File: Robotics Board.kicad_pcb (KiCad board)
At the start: 2 copper layers, 91 parts, among them CON1 DC_IN, J1 USB, K1 CONN_3, K2 CONN_3, P1 CONN_3, P10 CONN_6, P11 CONN_8, P12 CONN_12, P13 CONN_6, P14 CONN_12, P15 CONN_5, P16 CONN_12, P17 CONN_12, P18 CONN_12, P19 CONN_12, P2 CONN_3, P20 CONN_12, P21 CONN_12, P22 CONN_12, P23 CONN_1, P3 CONN_12, P4 CONN_12, P5 CONN_12, P6 CONN_12, P7 CONN_12, P8 CONN_8, P9 CONN_8, U1 7805, U2 L293, U3 PIC18F4550, U4 FT230X, X1 4MHz

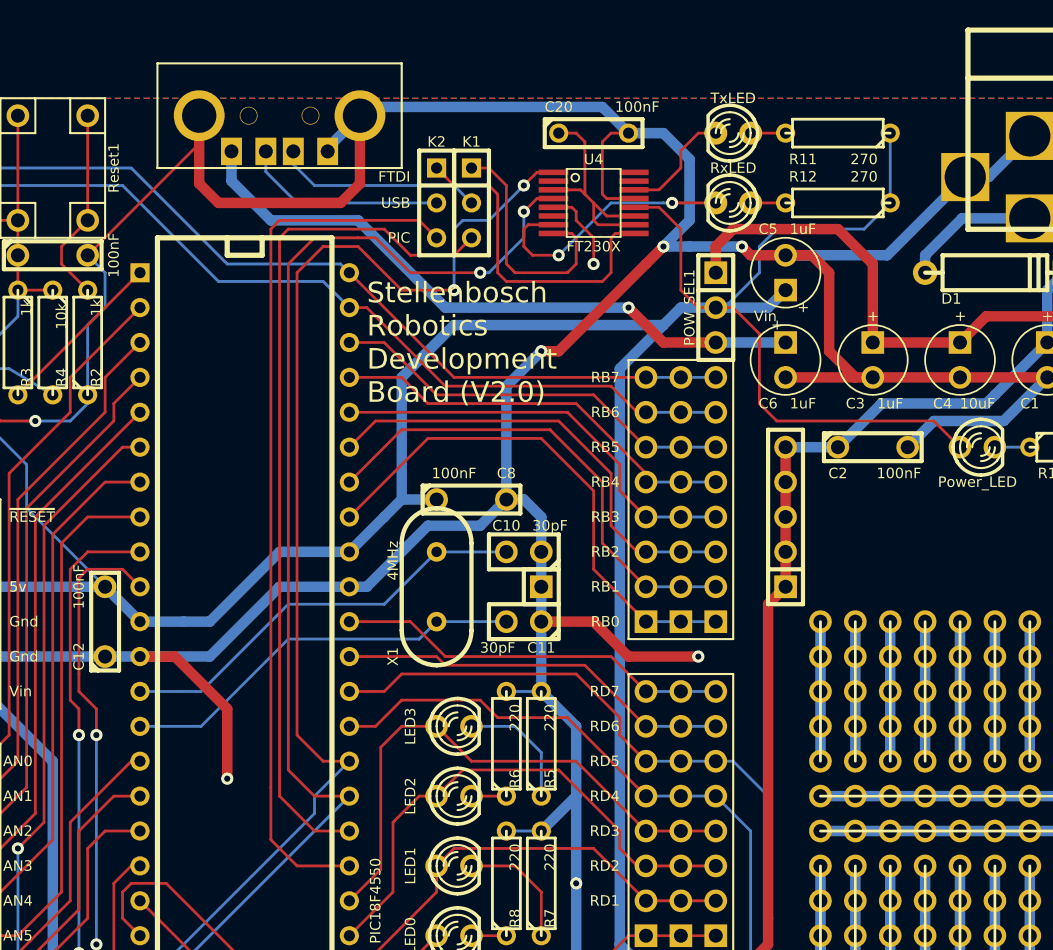
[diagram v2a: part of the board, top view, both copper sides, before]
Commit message: Eddited USB circuit to include resistors and capacitors.
Signed-off-by: Kolijn Wolfaardt <kolijn.wolfaardt@gmail.com>
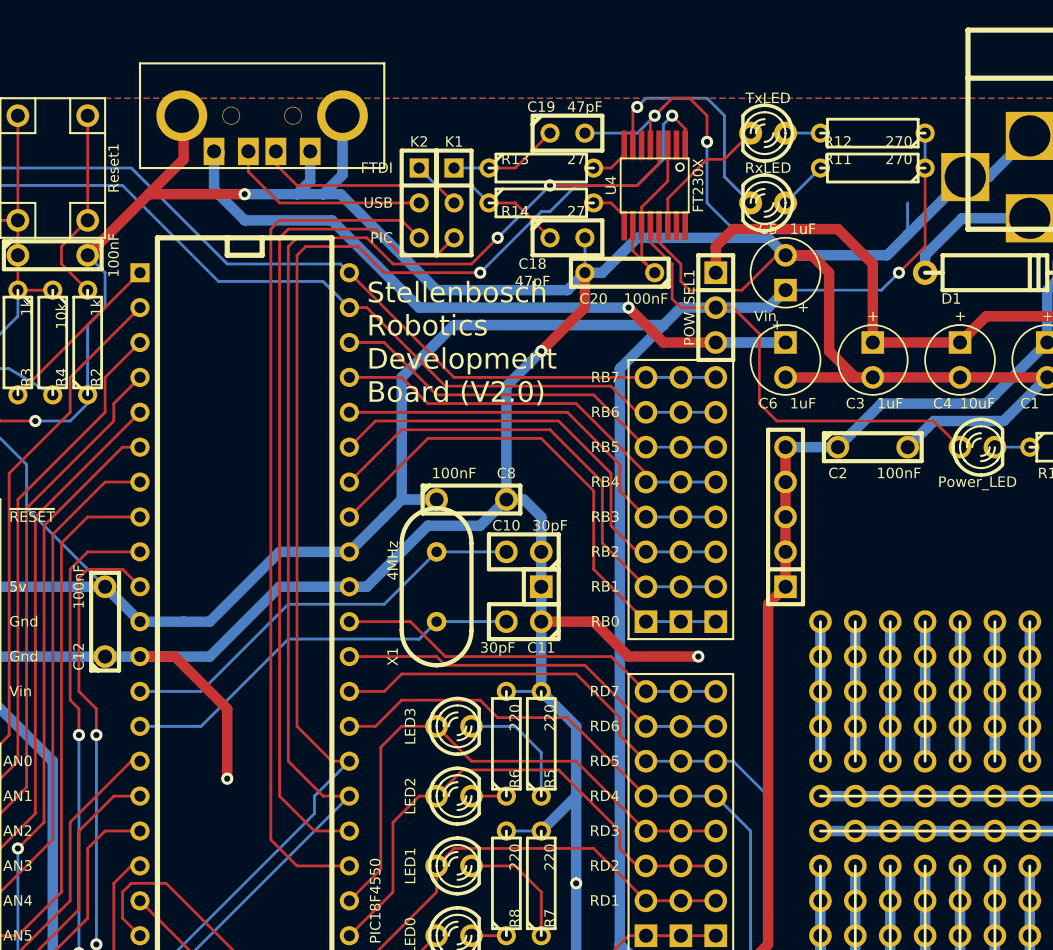
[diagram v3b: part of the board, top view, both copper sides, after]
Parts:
- added C18: 47pF, C1, F.Cu at (111.1, 62.2)
- added C19: 47pF, C1, F.Cu at (111.1, 54.6)
- added R13: 27, R3, F.Cu at (109.2, 57.1)
- added R14: 27, R3, F.Cu at (109.2, 59.7)
- moved C20 10.3 mm to (114.9, 64.8), turned to 180 degrees
- moved U4 4.62 mm to (117.5, 58.4), turned to 180 degrees
- moved R12 3.59 mm to (133.3, 57.1)
- moved D11 2.54 mm to (125.7, 54.6)
- moved D12 2.54 mm to (125.7, 59.7)
- moved R11 2.54 mm to (133.3, 54.6)
- moved J1 1.27 mm to (88.9, 53.3)
- moved K1 1.27 mm to (102.9, 59.7)
- moved K2 1.27 mm to (100.3, 59.7)
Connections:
- U4 pad 8: /Microcontroller/USB_D+ -> N-0000099
- U4 pad 9: /Microcontroller/USB_D- -> N-0000098
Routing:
- net Gnd: track 595.5 -> 611.4 mm
- net /Microcontroller/USB_D-: track 24.1 -> 11.6 mm
- net /Microcontroller/GP7: track 122.4 -> 133.5 mm
- net /Microcontroller/USB_D+: track 18.1 -> 8.04 mm
- net /Microcontroller/GP6: track 119.1 -> 127.9 mm
- net V_5v: track 345.4 -> 340.9 mm, vias 1 -> 2
- net N-0000098: track 0.00 -> 3.32 mm
- net N-0000099: track 0.00 -> 3.32 mm
- net /Microcontroller/VCCIO: track 16.9 -> 13.6 mm
- net /Microcontroller/CBUS2: track 19.4 -> 17.2 mm, vias 2 -> 1
- net /Microcontroller/CBUS1: track 8.42 -> 9.97 mm
- net /Microcontroller/PIC_USB_D+: track 62.3 -> 61.1 mm
- net /Microcontroller/PIC_USB_D-: track 63.8 -> 62.5 mm
- net Vbus: track 47.9 -> 49.2 mm
- net N-0000094: track 2.54 -> 3.59 mm

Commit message: Fixed some small errors
Signed-off-by: Kolijn Wolfaardt <kolijn.wolfaardt@gmail.com>
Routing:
- net V_5v: track 340.9 -> 333.1 mm
- net /Microcontroller/RB4: track 30.2 -> 32.7 mm
- net /Microcontroller/RB2: track 33.6 -> 36.2 mm
- net /Microcontroller/RB1: track 35.6 -> 38.1 mm
- net Gnd: track 611.4 -> 608.8 mm

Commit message: Changed the board to use 3.3v rather than 5v. Total new layout.
Since the FTDI chip cannot communicate with the 5v PIC. So run
the PIC at 3.3v This limits the maximum crystal frequency of
the pic, but 4MHz is fine. the internal usb regulator is no
longer used and is replaced with the external one.

The 3.3v regulator get it's 5v from the selected 5v source.
5v is still used by the FTDI chip and the Motor driver.

Signed-off-by: Kolijn Wolfaardt <kolijn.wolfaardt@gmail.com>
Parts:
- added C21: 100nF, C2, F.Cu at (106.7, 80.0)
- added C22: 100nF, C2, F.Cu at (83.8, 58.4)
- added P24: CONN_12, SIL-12, F.Cu at (143.5, 120.7)
- added R15: 18k, R3, F.Cu at (85.1, 61.0)
- added U5: 3.3VREG, LM78XXV-NumberedPads, F.Cu at (152.4, 80.0)
- C13: value 220nF -> 1uF; footprint C2 -> C1V5
- moved C13 79.4 mm to (146.1, 78.7), turned to 90 degrees
- moved C2 58.4 mm to (94.0, 120.7), turned to 180 degrees
- moved C7 33.9 mm to (110.5, 119.4)
- moved C8 33.2 mm to (71.1, 77.5)
- moved PWM2 33.0 mm to (82.5, 132.1), turned to 90 degrees
- moved C5 14.8 mm to (139.7, 78.7), turned to 90 degrees
- moved C9 9.74 mm to (119.4, 120.7), turned to 90 degrees
- moved D2 8.89 mm to (141.0, 86.4)
- moved R1 8.89 mm to (148.6, 86.4)
- moved D10 6.35 mm to (121.9, 133.3)
- moved D3 6.35 mm to (94.0, 128.3)
- moved D6 6.35 mm to (88.9, 133.3)
- moved D7 6.35 mm to (116.8, 128.3)
- moved P1 6.35 mm to (94.0, 144.8)
- moved P2 6.35 mm to (116.8, 144.8)
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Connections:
- C12 pad 2: V_5v -> V3.3
- C13 pad 1: /Microcontroller/Vusb -> V3.3
- C15 pad 1: V_5v -> V3.3
- C16 pad 1: V_5v -> V3.3
- C9 pad 2: V_5v -> V3.3
- ICSP1 pad 2: V_5v -> V3.3
- J1 pad 5: Gnd -> N-0000083
- J1 pad 6: Gnd -> N-0000083
- P13 pad 2: (no net) -> V3.3
- R10 pad 1: V_5v -> V3.3
- R11 pad 1: V_5v -> V3.3
- R12 pad 1: V_5v -> V3.3
- R4 pad 2: V_5v -> V3.3
- R9 pad 1: V_5v -> V3.3
- U3 pad 11: V_5v -> V3.3
- U3 pad 18: /Microcontroller/Vusb -> V3.3
- U3 pad 32: V_5v -> V3.3
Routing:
- net (no net): track 0.63 -> 3722.3 mm, vias 0 -> 27
- net V3.3: track 0.00 -> 326.9 mm, vias 0 -> 3
- net V_5v: track 333.1 -> 259.4 mm, vias 2 -> 3
- net Vbus: track 49.2 -> 71.5 mm, vias 1 -> 0
- net N-0000083: track 0.00 -> 21.1 mm
- net Gnd: track 608.8 -> 629.0 mm, vias 9 -> 6
- net N-0000073: track 12.5 -> 31.6 mm
- net N-0000074: track 14.3 -> 30.4 mm
- net V_batt: track 212.2 -> 198.2 mm, vias 1 -> 0
- net /Microcontroller/Vusb: track 13.1 -> 0.00 mm
- net N-0000071: track 41.9 -> 29.5 mm
- net /Microcontroller/RB6: track 73.2 -> 61.7 mm
- net /Microcontroller/RB7: track 71.8 -> 61.1 mm
- net /Microcontroller/GP6: track 127.9 -> 137.5 mm, vias 3 -> 1
- net /Microcontroller/RD1: track 56.2 -> 48.0 mm
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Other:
- board text added: "3.3v"

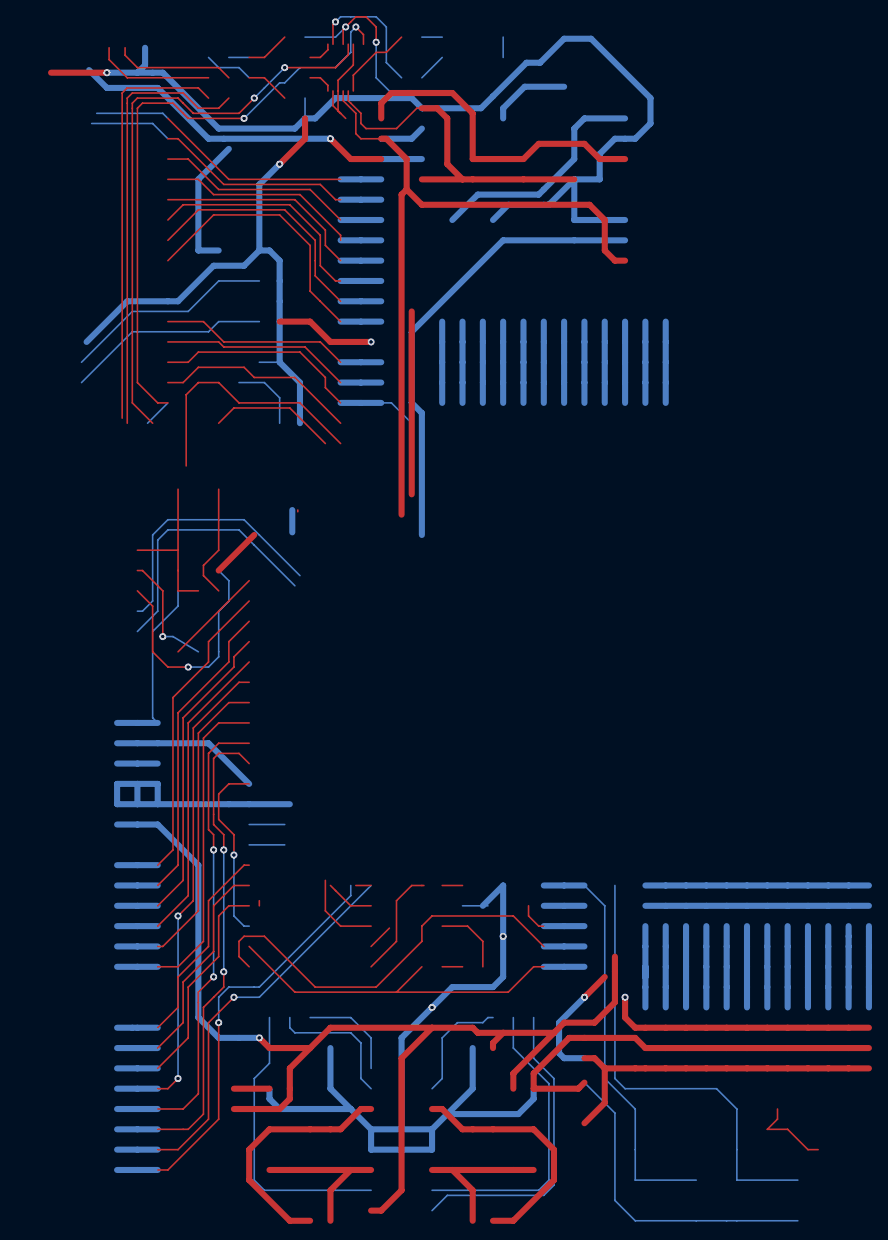
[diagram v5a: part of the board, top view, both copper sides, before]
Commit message: Removed unused tracks
Signed-off-by: Kolijn Wolfaardt <kolijn.wolfaardt@gmail.com>
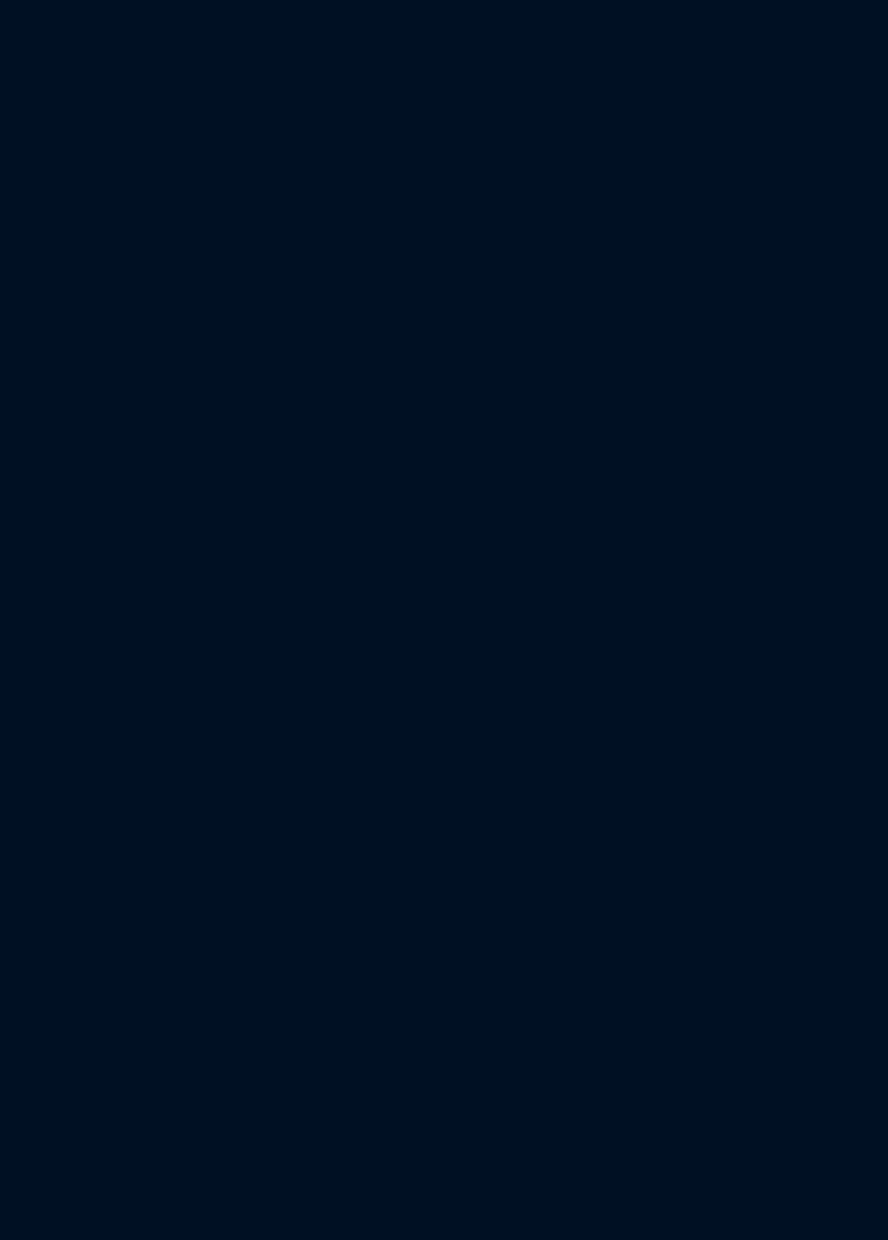
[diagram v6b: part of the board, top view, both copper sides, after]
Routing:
- net (no net): track 3722.3 -> 0.00 mm, vias 27 -> 0

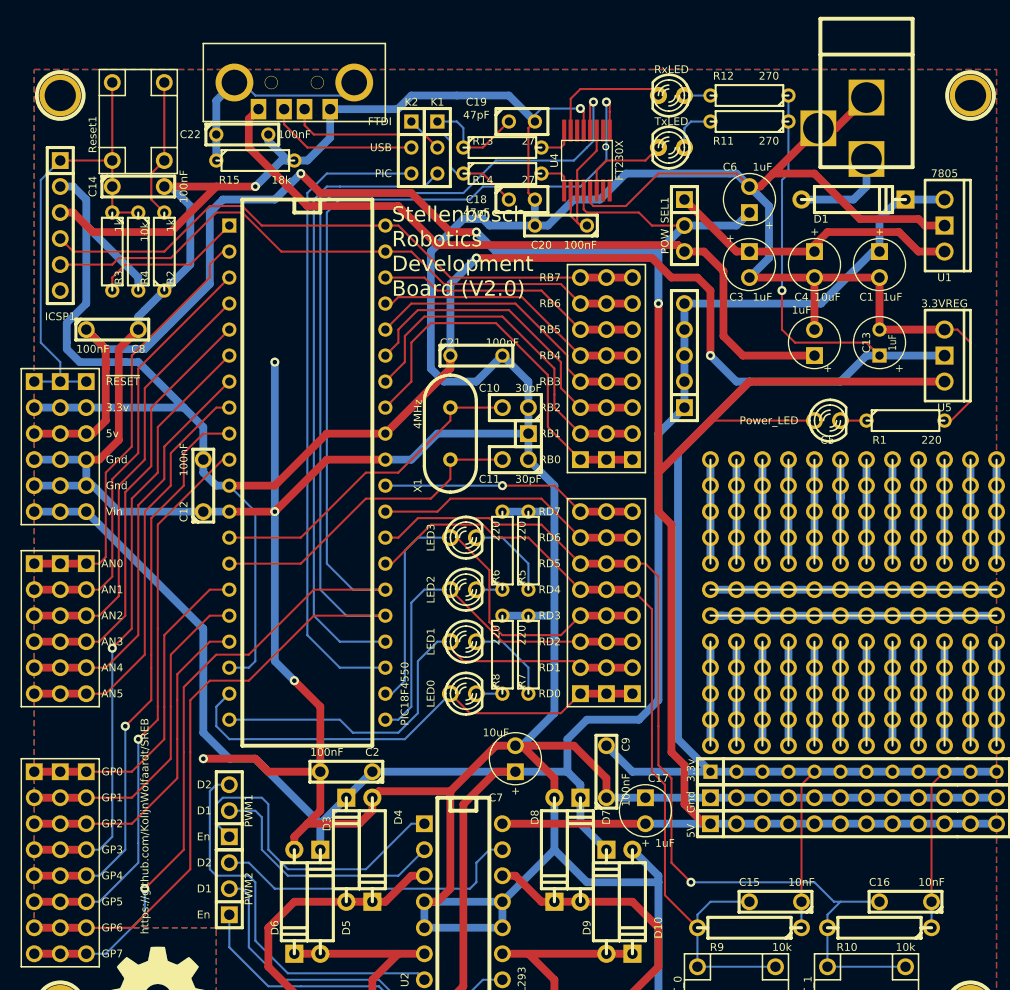
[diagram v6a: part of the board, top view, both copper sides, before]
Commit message: This branch uses a MCP2200 rather than an FTDI chip
Signed-off-by: Kolijn Wolfaardt <kolijn.wolfaardt@gmail.com>
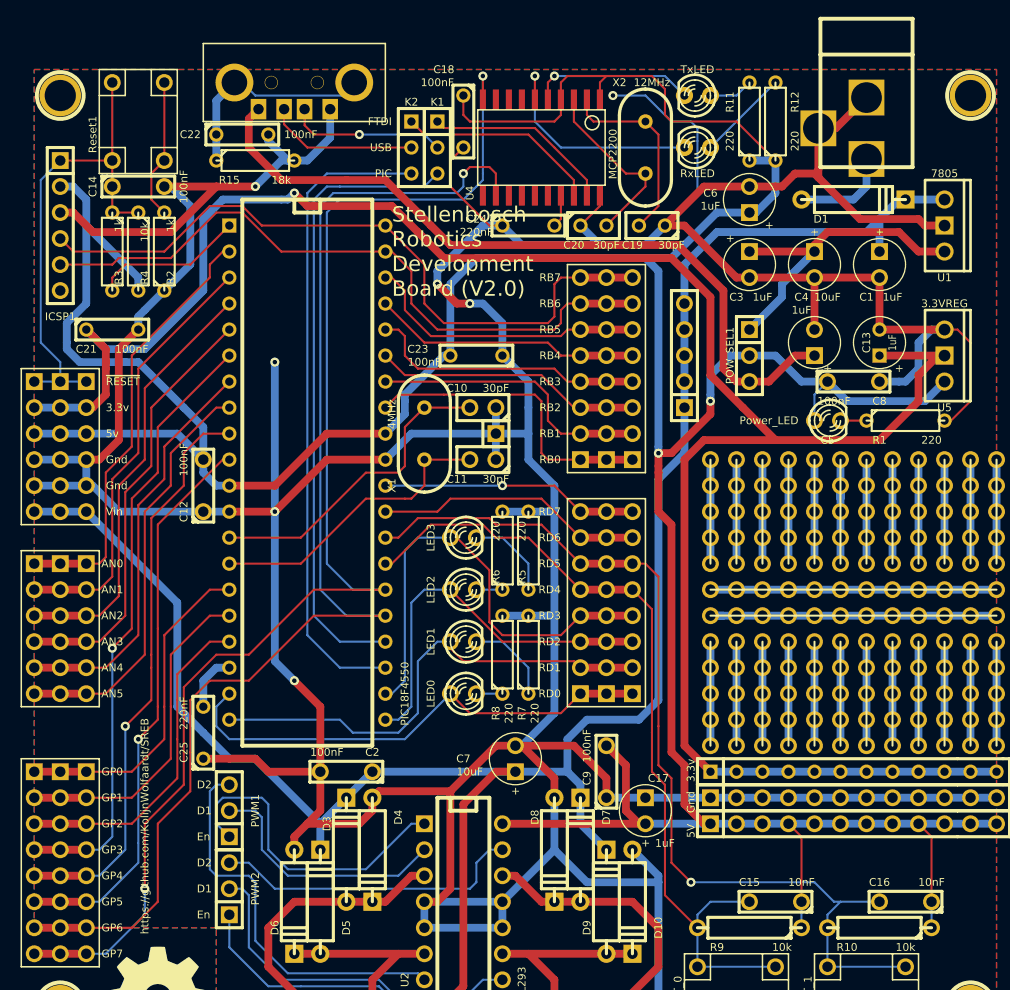
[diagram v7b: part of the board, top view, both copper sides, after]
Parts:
- removed R13, R14: 27, R3
- added C23: 100nF, C2, F.Cu at (106.7, 80.0)
- added C24: 220nF, C2, F.Cu at (111.8, 67.3)
- added C25: 220nF, C2, F.Cu at (80.0, 116.8)
- added X2: 12MHz, HC-49V, F.Cu at (123.2, 59.7)
- C18: value 47pF -> 100nF; footprint C1 -> C2
- C19: value 47pF -> 30pF
- C20: value 100nF -> 30pF; footprint C2 -> C1
- R11, R12: value 270 -> 220
- U4: value FT230X -> MCP2200; footprint ssop-16-extended -> so-20
- moved C8 72.6 mm to (143.5, 82.5)
- moved C21 35.7 mm to (71.1, 77.5)
- moved C19 16.3 mm to (123.8, 67.3), turned to 180 degrees
- moved POW_SEL1 14.2 mm to (133.3, 80.0)
- moved C18 9.53 mm to (105.4, 57.1), turned to 270 degrees
- moved D11 5.68 mm to (128.3, 54.6)
- moved D12 5.68 mm to (128.3, 59.7)
- moved R12 3.59 mm to (135.9, 57.1), turned to 90 degrees
- moved U4 3.42 mm to (114.3, 59.7)
- moved P23 3.18 mm to (108.6, 87.6)
- moved C10 3.17 mm to (107.3, 85.1)
- moved C11 3.17 mm to (107.3, 90.2)
- moved C20 3.17 mm to (118.1, 67.3), turned to 0 degrees
- moved X1 2.54 mm to (101.6, 87.6)
- turned R11 to 90 degrees
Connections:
- C12 pad 2: V3.3 -> V_5v
- C15 pad 1: V3.3 -> V_5v
- C16 pad 1: V3.3 -> V_5v
- C18 pad 1: /Microcontroller/USB_D- -> V_5v
- C19 pad 1: /Microcontroller/USB_D+ -> Gnd
- C19 pad 2: Gnd -> /Microcontroller/USB_OSC1
- C20 pad 1: /Microcontroller/VCCIO -> Gnd
- C20 pad 2: Gnd -> /Microcontroller/USB_OSC2
- C9 pad 2: V3.3 -> V_5v
- D11 pad 2: /Microcontroller/CBUS1 -> /Microcontroller/TxLED
- D12 pad 2: /Microcontroller/CBUS2 -> /Microcontroller/RxLED
- ICSP1 pad 2: V3.3 -> V_5v
- R10 pad 1: V3.3 -> V_5v
- R11 pad 1: V3.3 -> V_5v
- R12 pad 1: V3.3 -> V_5v
- R4 pad 2: V3.3 -> V_5v
- R9 pad 1: V3.3 -> V_5v
- U3 pad 11: V3.3 -> V_5v
- U3 pad 18: V3.3 -> /Microcontroller/VUSB
- U3 pad 32: V3.3 -> V_5v
- U4 pad 1: /Microcontroller/GP7 -> V_5v
- U4 pad 10: /Microcontroller/VCCIO -> /Microcontroller/GP7
- U4 pad 11: /Microcontroller/VCCIO -> (no net)
- U4 pad 12: V_5v -> /Microcontroller/GP6
- U4 pad 13: Gnd -> (no net)
- U4 pad 14: /Microcontroller/CBUS1 -> (no net)
- U4 pad 2: (no net) -> /Microcontroller/USB_OSC1
- U4 pad 3: /Microcontroller/VCCIO -> /Microcontroller/USB_OSC2
- U4 pad 4: /Microcontroller/GP6 -> V_5v
- U4 pad 5: Gnd -> /Microcontroller/TxLED
- U4 pad 6: (no net) -> /Microcontroller/RxLED
- U4 pad 7: /Microcontroller/CBUS2 -> (no net)
- U4 pad 8: N-0000090 -> (no net)
- U4 pad 9: N-0000089 -> (no net)
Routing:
- net V3.3: track 326.9 -> 204.5 mm, vias 3 -> 1
- net V_5v: track 259.4 -> 366.9 mm, vias 3 -> 2
- net /Microcontroller/RxLED: track 0.00 -> 22.4 mm, vias 0 -> 1
- net /Microcontroller/USB_OSC1: track 0.00 -> 19.0 mm
- net /Microcontroller/USB_OSC2: track 0.00 -> 17.9 mm
- net /Microcontroller/VCCIO: track 16.5 -> 0.00 mm
- net /Microcontroller/TxLED: track 0.00 -> 16.0 mm, vias 0 -> 1
- net Gnd: track 629.0 -> 614.2 mm, vias 6 -> 7
- net /Microcontroller/GP6: track 137.5 -> 123.3 mm
- net /Microcontroller/CBUS2: track 12.3 -> 0.00 mm
- net /Microcontroller/GP7: track 138.9 -> 129.9 mm
- net /Microcontroller/CBUS1: track 8.92 -> 0.00 mm
- net /Microcontroller/USB_D+: track 10.2 -> 18.5 mm
- net /Microcontroller/RB0: track 38.3 -> 30.3 mm
- net /Microcontroller/RB7: track 61.1 -> 68.9 mm
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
